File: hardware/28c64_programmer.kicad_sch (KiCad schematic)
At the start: 12 parts, among them U1 74HC595 (A0-A7), U2 74HC595 (A8-A12), U3 AT28C64B-15PC

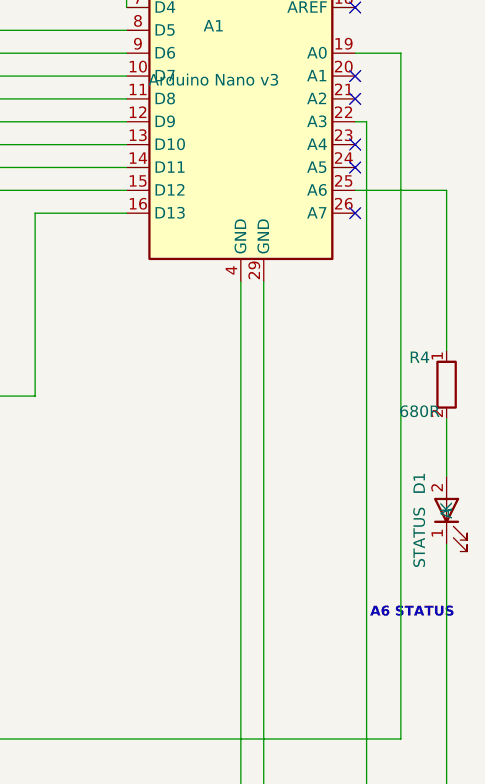
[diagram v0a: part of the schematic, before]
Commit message: hardware: update wired schematic for A5 LED
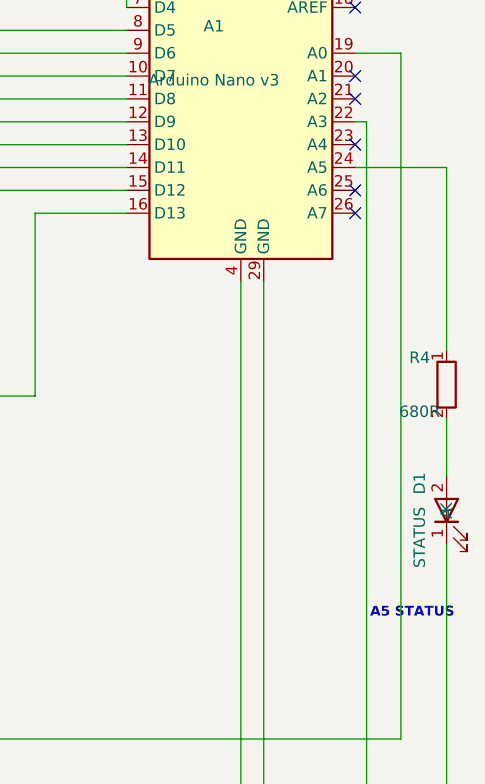
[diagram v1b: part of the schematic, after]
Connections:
- net at A1.24 (A5): now also R4.1
- net at A1.25 (A6): no longer R4.1
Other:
- note added: "A5 STATUS"
- note removed: "A6 STATUS"
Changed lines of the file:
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@@
 		(comment 1 "Protected writes; reset-safe controlled /CE")
-	)
-	(text "A6 STATUS"
-		(exclude_from_sim no)
-		(at 274.32 137.16 0)
-		(effects
-			(font
-				(size 1.1 1.1)
-				(bold yes)
-			)
-		)
 	)
 	(text "/CE is controlled by A3 and pulled high. Never tie /CE to GND when /WE uses D13."
@@
 		)
 	)
+	(text "A5 STATUS"
+		(exclude_from_sim no)
+		(at 274.32 137.16 0)
+		(effects
+			(font
+				(size 1.1 1.1)
+				(bold yes)
+			)
+		)
+	)
 	(text "BYPASS CAPACITORS"
 		(exclude_from_sim no)
@@
 	)
 	(no_connect
-		(at 267.97 87.63)
-	)
-	(no_connect
 		(at 130.81 142.24)
 	)
@@
 	)
 	(no_connect
+		(at 267.97 90.17)
+	)
+	(no_connect
 		(at 252.73 49.53)
 	)
@@
 	(wire
 		(pts
+			(xy 278.13 87.63) (xy 278.13 107.95)
+		)
+		(stroke
+			(width 0)
+			(type default)
+		)
+	)
+	(wire
+		(pts
 			(xy 60.96 38.1) (xy 260.35 38.1)
 		)
@@
 	(wire
 		(pts
-			(xy 267.97 90.17) (xy 278.13 90.17)
-		)
-		(stroke
-			(width 0)
-			(type default)
-		)
-	)
-	(wire
-		(pts
 			(xy 267.97 82.55) (xy 269.24 82.55)
 		)
@@
 	(wire
 		(pts
+			(xy 267.97 87.63) (xy 278.13 87.63)
+		)
+		(stroke
+			(width 0)
+			(type default)
+		)
+	)
+	(wire
+		(pts
 			(xy 237.49 64.77) (xy 237.49 54.61)
 		)
 		(stroke
-			(width 0)
-			(type default)
-		)
-	)
-	(wire
-		(pts
-			(xy 278.13 90.17) (xy 278.13 107.95)
-		)
-		(stroke

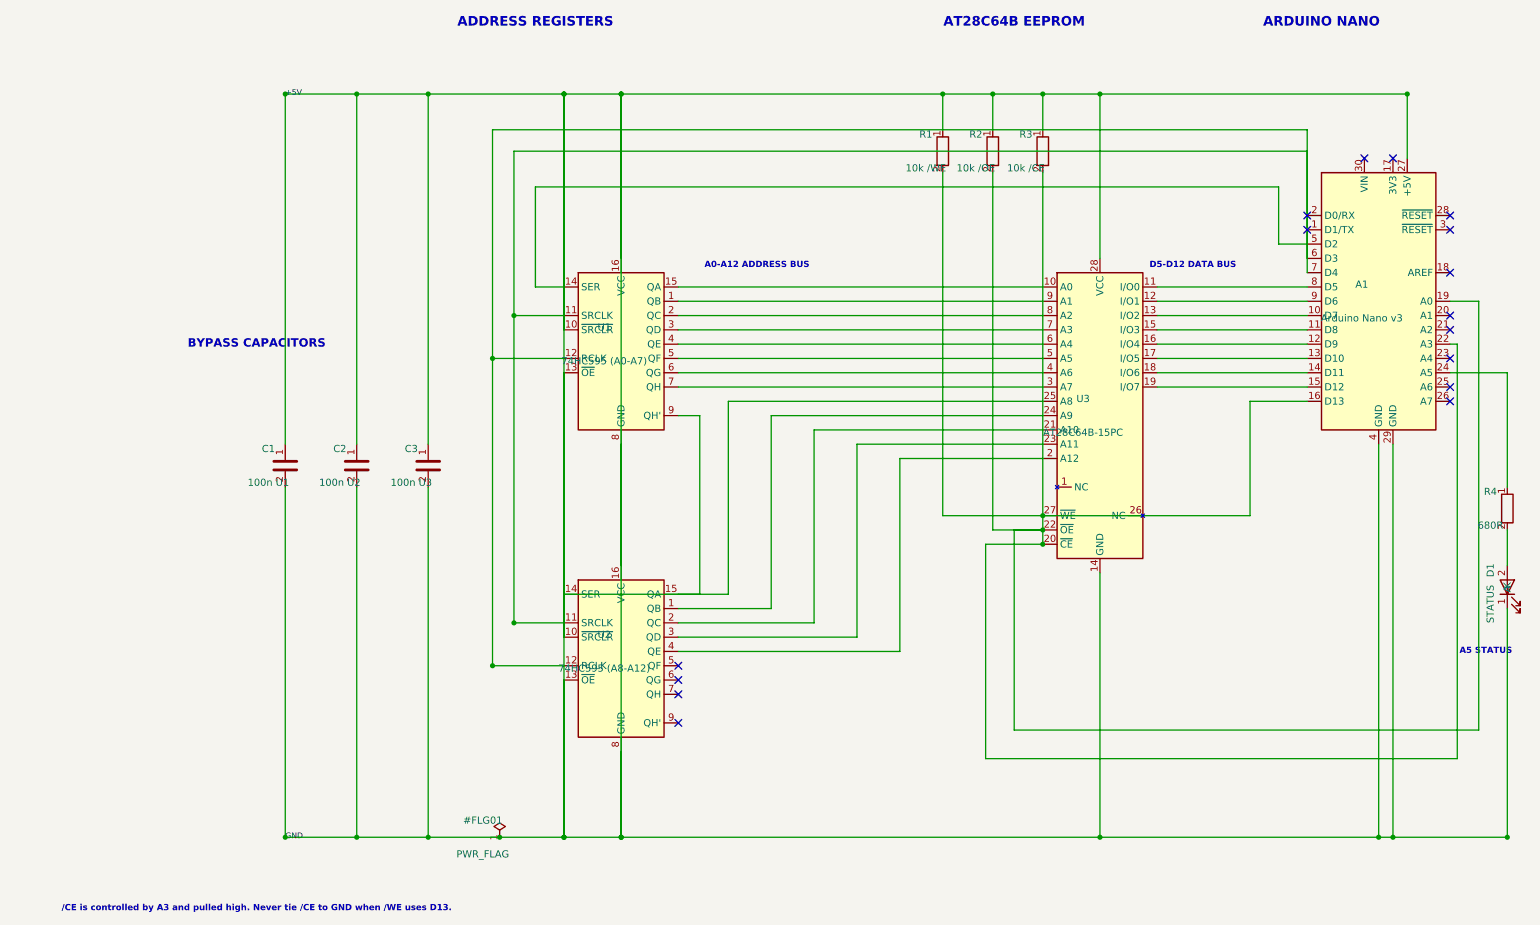
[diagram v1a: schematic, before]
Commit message: hardware: clarify component labels and values
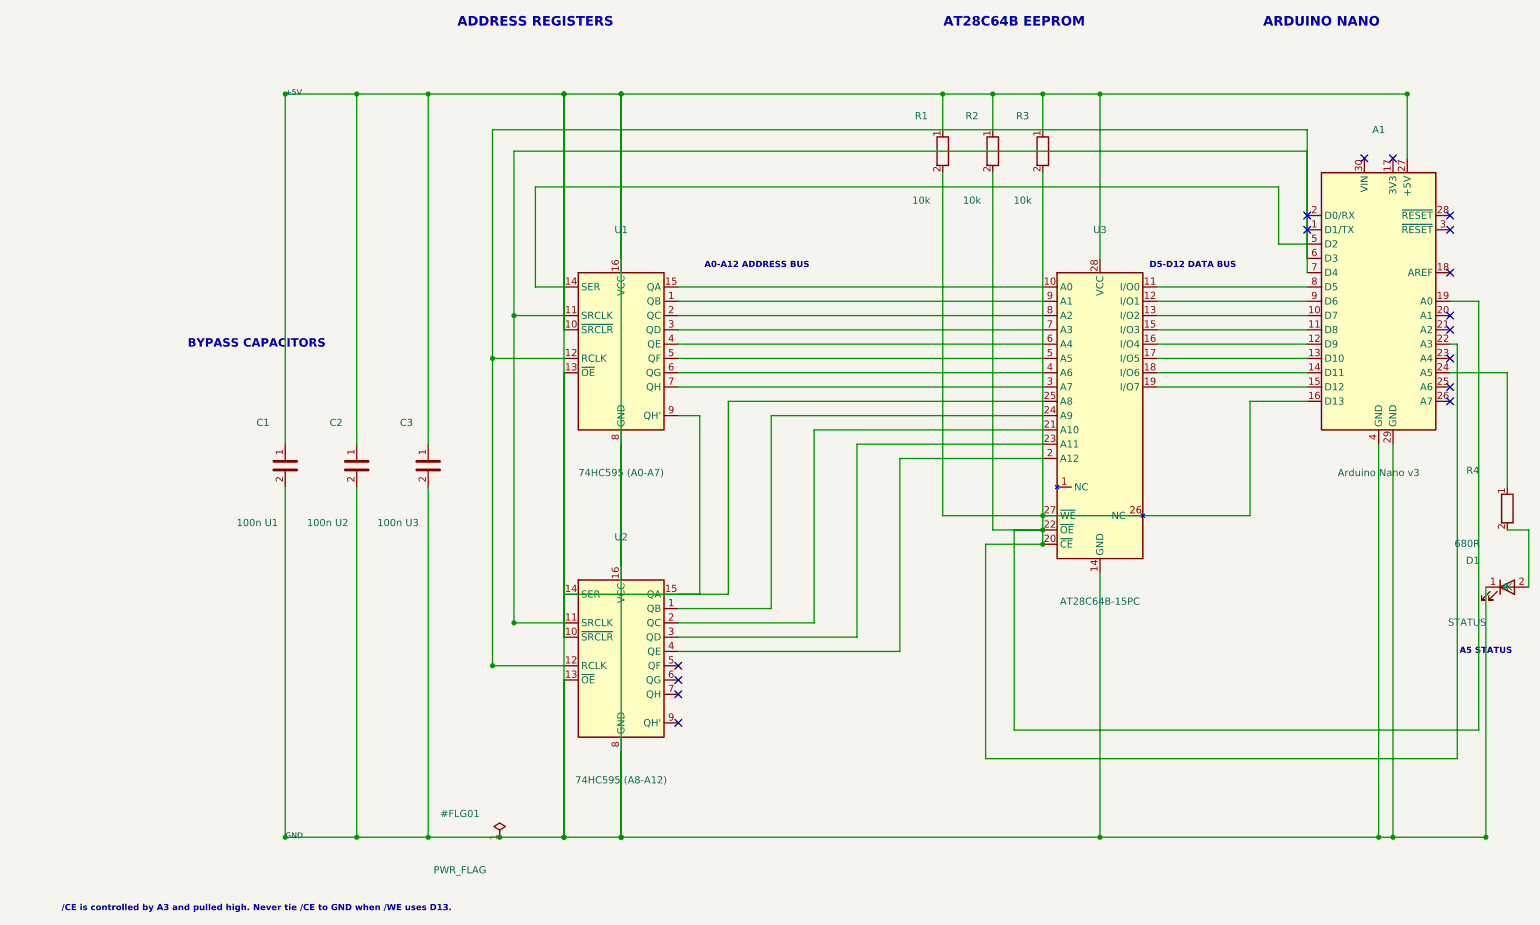
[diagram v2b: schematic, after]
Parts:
- R1: value 10k /WE -> 10k
- R2: value 10k /OE -> 10k
- R3: value 10k /CE -> 10k
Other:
- moved on the sheet: D1
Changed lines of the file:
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@@
-	)
-	(junction
-		(at 278.13 170.18)
-		(diameter 0)
-		(color 0 0 0 0)
 	)
 	(junction
@@
 	)
 	(junction
+		(at 274.32 170.18)
+		(diameter 0)
+		(color 0 0 0 0)
+	)
+	(junction
 		(at 73.66 170.18)
 		(diameter 0)
@@
 	(wire
 		(pts
-			(xy 278.13 115.57) (xy 278.13 121.92)
-		)
-		(stroke
-			(width 0)
-			(type default)
-		)
-	)
-	(wire
-		(pts
 			(xy 120.65 100.33) (xy 120.65 170.18)
 		)
@@
 	(wire
 		(pts
-			(xy 278.13 129.54) (xy 278.13 170.18)
-		)
-		(stroke
-			(width 0)
-			(type default)
-		)
-	)
-	(wire
-		(pts
 			(xy 134.62 95.25) (xy 134.62 127)
 		)
@@
 	(wire
 		(pts
+			(xy 278.13 115.57) (xy 281.94 115.57)
+		)
+		(stroke
+			(width 0)
+			(type default)
+		)
+	)
+	(wire
+		(pts
 			(xy 215.9 87.63) (xy 242.57 87.63)
 		)
@@
 	(wire
 		(pts
+			(xy 60.96 170.18) (xy 274.32 170.18)
+		)
+		(stroke
+			(width 0)
+			(type default)
+		)
+	)
+	(wire
+		(pts
 			(xy 134.62 127) (xy 110.49 127)
 		)
@@
 	(wire
 		(pts
-			(xy 60.96 170.18) (xy 278.13 170.18)
-		)
-		(stroke
-			(width 0)
-			(type default)
-		)
-	)
-	(wire
-		(pts
 			(xy 147.32 95.25) (xy 195.58 95.25)
 		)
@@
 	(wire
 		(pts
+			(xy 274.32 125.73) (xy 274.32 170.18)
+		)
+		(stroke
+			(width 0)
+			(type default)
+		)
+	)
+	(wire
+		(pts
 			(xy 86.36 107.95) (xy 86.36 170.18)
 		)
@@
 		(pts
 			(xy 120.65 121.92) (xy 120.65 38.1)
+		)
+		(stroke
+			(width 0)
+			(type default)
+		)
+	)
+	(wire
+		(pts
+			(xy 281.94 115.57) (xy 281.94 125.73)
 		)
 		(stroke
@@
 		(dnp no)
 		(property "Reference" "U1"
-			(at 117.65 79.55 0)
+			(at 120.65 62.23 0)
 			(show_name no)
 			(do_not_autoplace no)
@@
 		)
 		(property "Value" "74HC595 (A0-A7)"
-			(at 117.65 85.55 0)
+			(at 120.65 105.41 0)
 			(show_name no)
 			(do_not_autoplace no)
@@
 		(dnp no)
 		(property "Reference" "U2"
-			(at 117.65 134.16 0)
+			(at 120.65 116.84 0)
 			(show_name no)
 			(do_not_autoplace no)
@@
 		)
 		(property "Value" "74HC595 (A8-A12)"
-			(at 117.65 140.16 0)
+			(at 120.65 160.02 0)
 			(show_name no)
 			(do_not_autoplace no)
@@
 		(dnp no)
 		(property "Reference" "A1"
-			(at 252.27 71.93 0)
+			(at 255.27 44.45 0)
 			(show_name no)
 			(do_not_autoplace no)
@@
 		)
 		(property "Value" "Arduino Nano v3"
-			(at 252.27 77.93 0)
+			(at 255.27 105.41 0)
 			(show_name no)
 			(do_not_autoplace no)
@@
 		(dnp no)
 		(property "Reference" "U3"
-			(at 202.74 92.25 0)
+			(at 205.74 62.23 0)
 			(show_name no)
 			(do_not_autoplace no)
@@
 		)
 		(property "Value" "AT28C64B-15PC"
-			(at 202.74 98.25 0)
+			(at 205.74 128.27 0)
 			(show_name no)
 			(do_not_autoplace no)
@@
 		(dnp no)
 		(property "Reference" "R1"
-			(at 174.8 45.26 0)
-			(show_name no)
-			(do_not_autoplace no)
-			(effects
-				(font
-					(size 1.27 1.27)
-				)
-			)
-		)
-		(property "Value" "10k /WE"
-			(at 174.8 51.26 0)
+			(at 174 42 0)
+			(show_name no)
+			(do_not_autoplace no)
+			(effects
+				(font
+					(size 1.27 1.27)
+				)
+			)
+		)
+		(property "Value" "10k"
+			(at 174 57 0)
 			(show_name no)
 			(do_not_autoplace no)
@@
 		(dnp no)
 		(property "Reference" "#FLG01"
-			(at 96.06 167.18 0)
+			(at 92 166 0)
 			(show_name no)
 			(do_not_autoplace no)
@@
 		)
 		(property "Value" "PWR_FLAG"
-			(at 96.06 173.18 0)
+			(at 92 176 0)
 			(show_name no)
 			(do_not_autoplace no)
@@
 		(dnp no)
 		(property "Reference" "C3"
-			(at 83.36 101.14 0)
+			(at 82.5 96.5 0)
 			(show_name no)
 			(do_not_autoplace no)
@@
 		)
 		(property "Value" "100n U3"
-			(at 83.36 107.14 0)
+			(at 81 114.3 0)
 			(show_name no)
 			(do_not_autoplace no)
@@
 		(dnp no)
 		(property "Reference" "C1"
-			(at 57.96 101.14 0)
+			(at 57 96.5 0)
 			(show_name no)
 			(do_not_autoplace no)
@@
 		)
 		(property "Value" "100n U1"
-			(at 57.96 107.14 0)
+			(at 56 114.3 0)
 			(show_name no)
 			(do_not_autoplace no)
@@
 		(dnp no)
 		(property "Reference" "R3"
-			(at 192.58 45.26 0)
-			(show_name no)
-			(do_not_autoplace no)
-			(effects
-				(font
-					(size 1.27 1.27)
-				)
-			)
-		)
-		(property "Value" "10k /CE"
-			(at 192.58 51.26 0)
+			(at 192 42 0)
+			(show_name no)
+			(do_not_autoplace no)
+			(effects
+				(font
+					(size 1.27 1.27)
+				)
+			)
+		)
+		(property "Value" "10k"
+			(at 192 57 0)
 			(show_name no)
 			(do_not_autoplace no)
@@
 	(symbol
 		(lib_id "Device:LED")
-		(at 278.13 125.73 90)
+		(at 278.13 125.73 0)
 		(unit 1)
 		(body_style 1)
@@
 		(dnp no)
 		(property "Reference" "D1"
-			(at 275.13 122.73 0)
+			(at 272 121 0)
 			(show_name no)
 			(do_not_autoplace no)
@@
 		)
 		(property "Value" "STATUS"
-			(at 275.13 128.73 0)
+			(at 271 132 0)
 			(show_name no)
 			(do_not_autoplace no)
@@
 		(dnp no)
 		(property "Reference" "R4"
-			(at 275.13 108.76 0)
+			(at 272 105 0)
 			(show_name no)
 			(do_not_autoplace no)
@@
 		)
 		(property "Value" "680R"
-			(at 275.13 114.76 0)
+			(at 271 118 0)
 			(show_name no)
 			(do_not_autoplace no)
@@
 		(dnp no)
 		(property "Reference" "C2"
-			(at 70.66 101.14 0)
+			(at 70 96.5 0)
 			(show_name no)
 			(do_not_autoplace no)
@@
 		)
 		(property "Value" "100n U2"
-			(at 70.66 107.14 0)
+			(at 68.5 114.3 0)
 			(show_name no)
 			(do_not_autoplace no)
@@
 		(dnp no)
 		(property "Reference" "R2"
-			(at 183.69 45.26 0)
-			(show_name no)
-			(do_not_autoplace no)
-			(effects
-				(font
-					(size 1.27 1.27)
-				)
-			)
-		)
-		(property "Value" "10k /OE"
-			(at 183.69 51.26 0)
-			(show_name no)
-			(do_not_autoplace no)
+			(at 183 42 0)
+			(show_name no)
+			(do_not_autoplace no)
+			(effects
+				(font
+					(size 1.27 1.27)
+				)
+			)
+		)
+		(property "Value" "10k"
+			(at 183 57 0)
+			(show_name no)
+			(do_not_autoplace no)

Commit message: hardware: apply Nano28C64 schematic title
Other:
- title: Arduino Nano AT28C64B Programmer -> Nano28C64 — Arduino Nano AT28C64B Programmer
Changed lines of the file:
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@@
 	(paper "A4")
 	(title_block
-		(title "Arduino Nano AT28C64B Programmer")
+		(title "Nano28C64 — Arduino Nano AT28C64B Programmer")
 		(date "2026-10-11")
 		(rev "v10")
